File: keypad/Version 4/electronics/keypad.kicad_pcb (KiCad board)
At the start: 4 copper layers, 39.9 x 39.9 mm, 35 parts, among them J1 USB_B_Micro, J2 Ext-Batt, J3 IO-Con, J4 Conn_01x06_Pin, J5 IO-Con, SW1 Ident, U1 PY32F003F18P6TU, U2 TP4054, U3 XC6206P332MR, U4 NRF24L01_SMD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

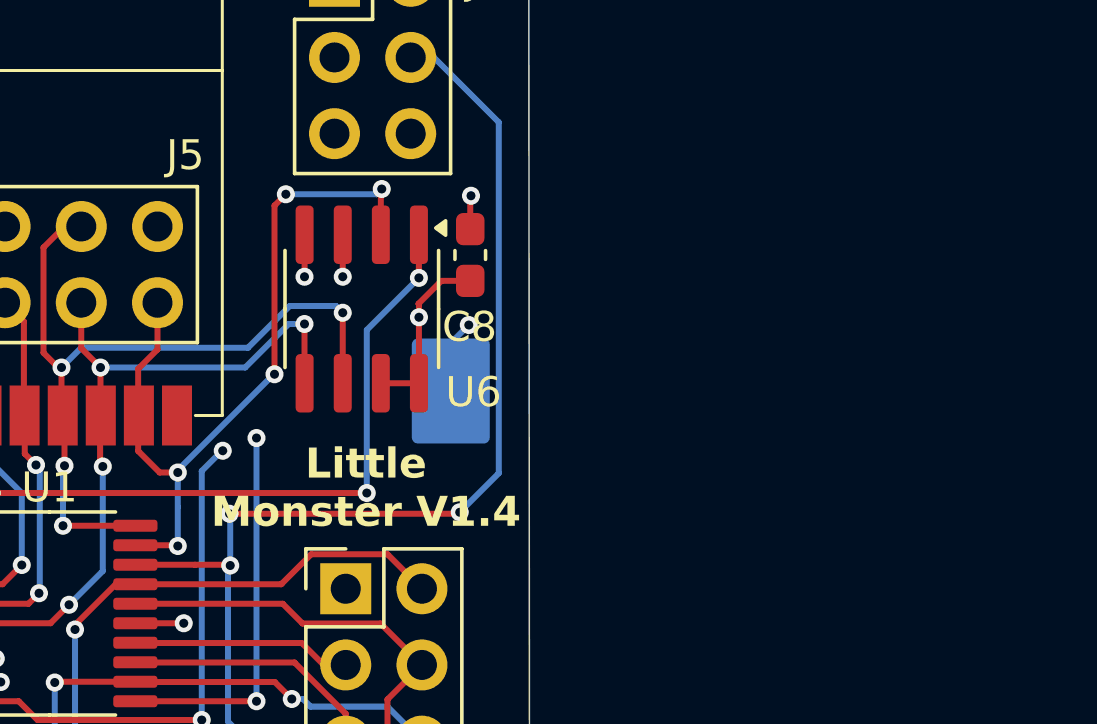
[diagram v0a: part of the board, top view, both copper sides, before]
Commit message: Flash code added and littlefs
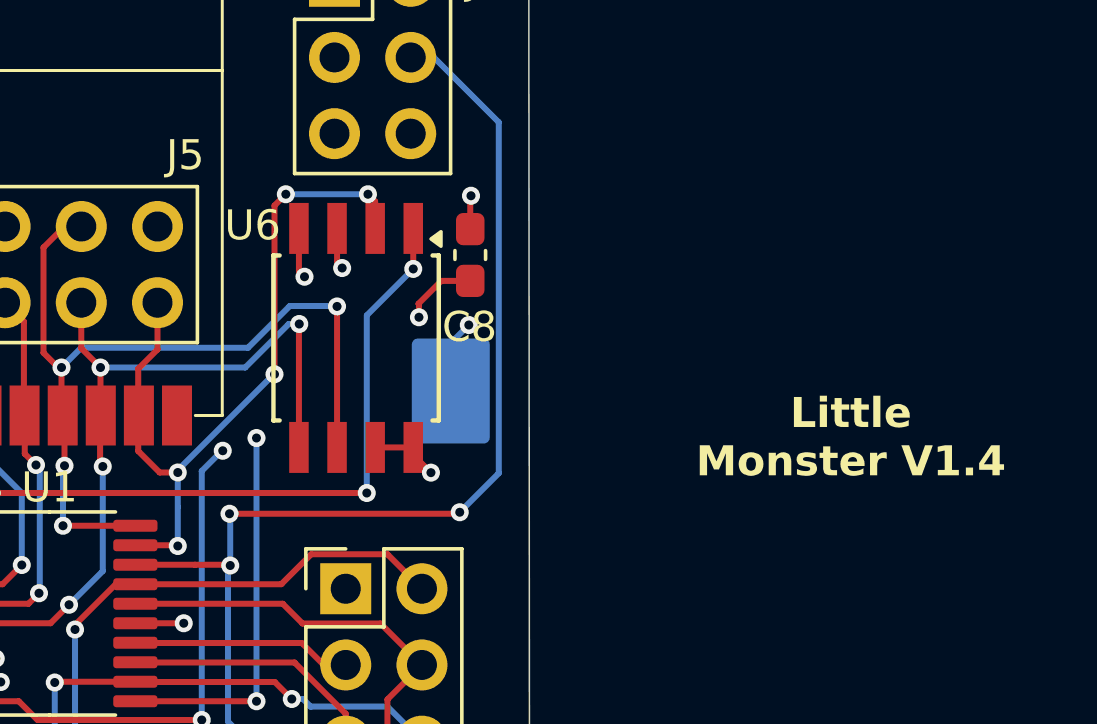
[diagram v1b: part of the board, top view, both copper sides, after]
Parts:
- U6: footprint Package_SO:SOIC-8_3.9x4.9mm_P1.27mm -> Package_SO:SOIC-8W_5.3x5.3mm_P1.27mm
- moved U6 0.98 mm to (150.7, 95.6)
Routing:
- net /SCK: track 26.3 -> 28.4 mm
- net /MOSI: track 24.0 -> 26.0 mm
- net +3V3: track 29.3 -> 28.1 mm, vias 6 -> 7
- net /MISO: track 26.3 -> 25.5 mm

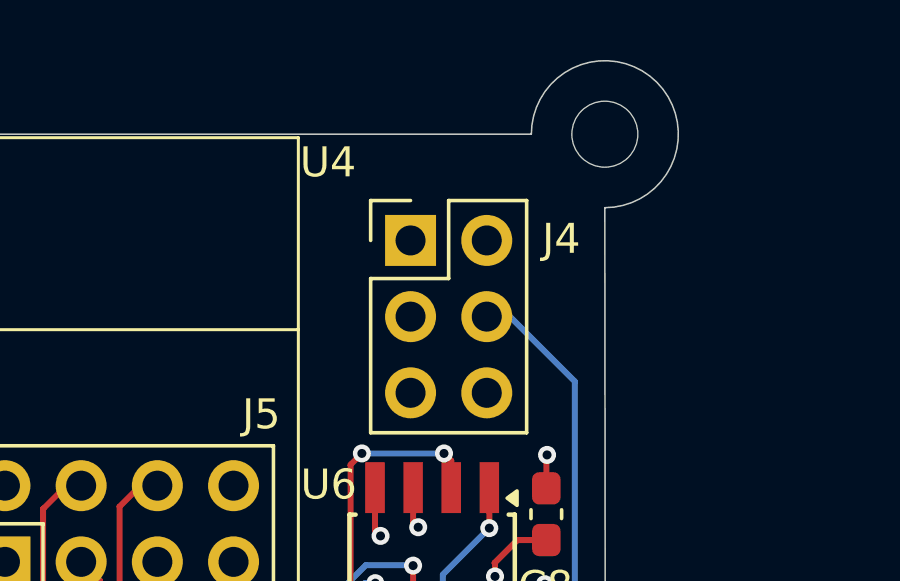
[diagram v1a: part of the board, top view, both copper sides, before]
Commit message: Added basic interpreter (untested)  now adding forth
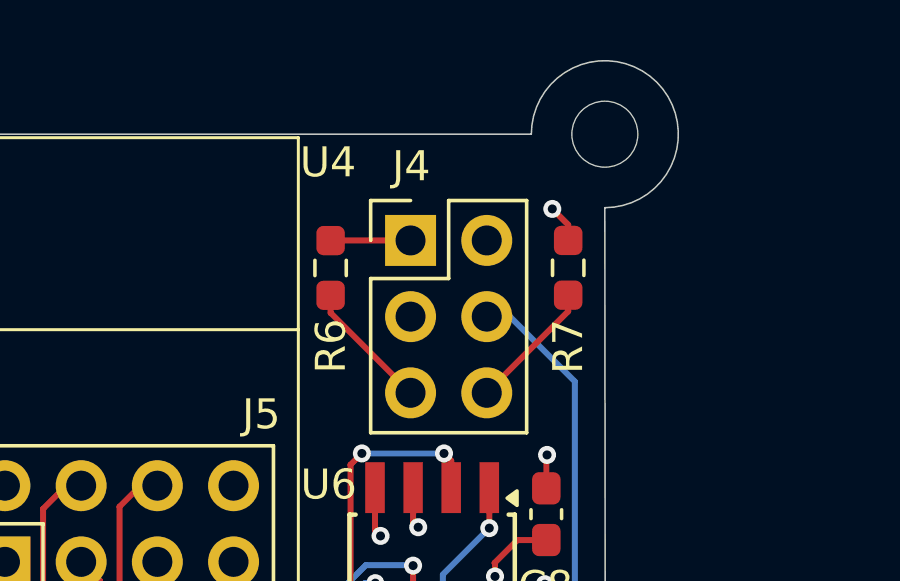
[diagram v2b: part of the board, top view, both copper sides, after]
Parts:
- added R6: 100k, Resistor_SMD:R_0603_1608Metric_Pad0.98x0.95mm_HandSolder, F.Cu at (147.3, 84.6)
- added R7: 100k, Resistor_SMD:R_0603_1608Metric_Pad0.98x0.95mm_HandSolder, F.Cu at (155.2, 84.6)
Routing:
- net /SWC: track 26.9 -> 31.3 mm
- net /SWD: track 30.7 -> 35.0 mm
- net +3V3: track 28.1 -> 32.1 mm, vias 7 -> 8
